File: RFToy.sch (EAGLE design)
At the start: 33 parts, among them IC1 ATMEGA328P, IC4 CH340G, J1 AYZ0202, X1 USBSMD, X2 12MHz

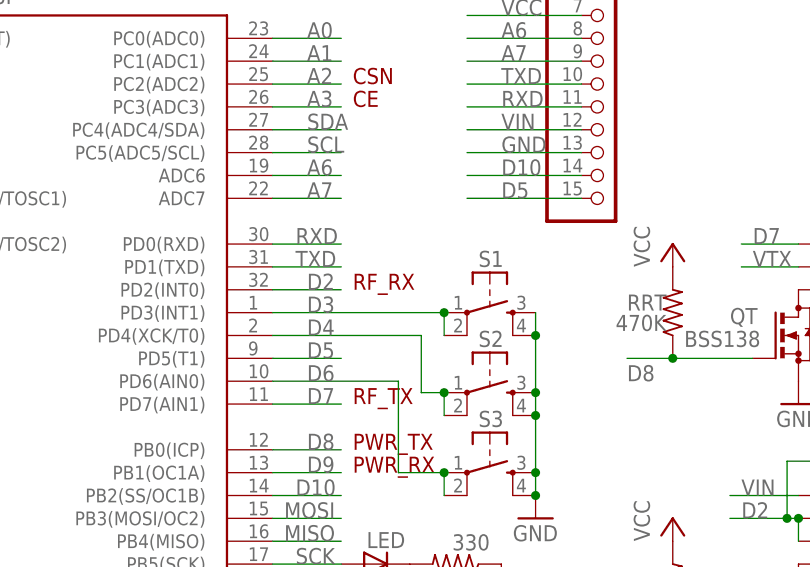
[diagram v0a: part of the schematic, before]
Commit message: correct pin assignments
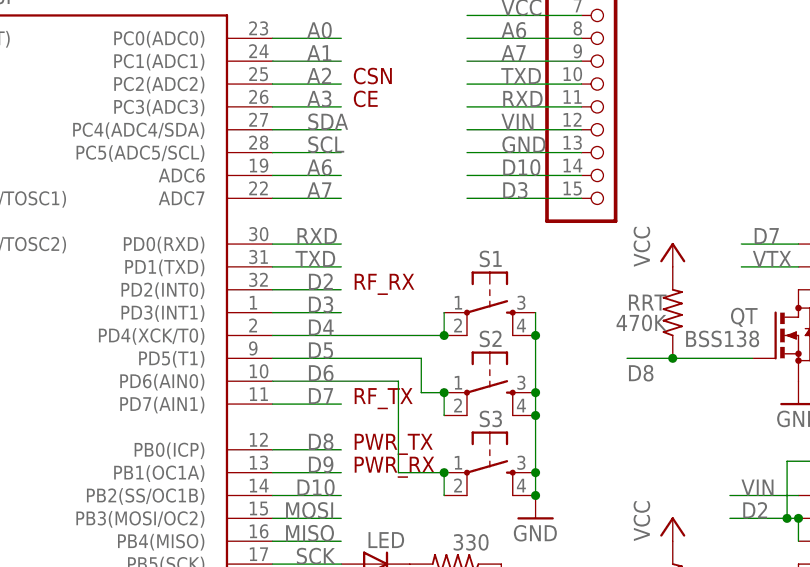
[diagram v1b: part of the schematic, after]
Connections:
- net D3: now also JP6.15; no longer S1.1, S1.2
- net D4: now also S1.1, S1.2; no longer S2.1, S2.2
- net D5: now also S2.1, S2.2; no longer JP6.15
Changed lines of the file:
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@@
 <setting verticaltext="up"/>
 </settings>
-<grid distance="0.05" unitdist="inch" unit="inch" style="lines" multiple="1" display="no" altdistance="0.01" altunitdist="inch" altunit="inch"/>
+<grid distance="0.1" unitdist="inch" unit="inch" style="lines" multiple="1" display="no" altdistance="0.01" altunitdist="inch" altunit="inch"/>
 <layers>
 <layer number="1" name="Top" color="4" fill="1" visible="no" active="no"/>
@@
 <pinref part="S3" gate="S" pin="4"/>
 <junction x="91.44" y="11.43"/>
-<wire x1="91.44" y1="31.75" x2="91.44" y2="29.21" width="0.1524" layer="91"/>
 <pinref part="S1" gate="S" pin="3"/>
 <pinref part="S1" gate="S" pin="4"/>
+<wire x1="91.44" y1="31.75" x2="91.44" y2="29.21" width="0.1524" layer="91"/>
 <wire x1="91.44" y1="29.21" x2="91.44" y2="22.86" width="0.1524" layer="91"/>
 <junction x="91.44" y="29.21"/>
@@
 </segment>
 </net>
-<net name="D4" class="0">
-<segment>
-<pinref part="IC1" gate="G$1" pin="PD4(XCK/T0)"/>
-<label x="66.04" y="29.21" size="1.778" layer="95"/>
-<wire x1="62.23" y1="29.21" x2="78.74" y2="29.21" width="0.1524" layer="91"/>
-<wire x1="78.74" y1="29.21" x2="78.74" y2="22.86" width="0.1524" layer="91"/>
-<wire x1="81.28" y1="22.86" x2="81.28" y2="20.32" width="0.1524" layer="91"/>
-<pinref part="S2" gate="S" pin="1"/>
-<pinref part="S2" gate="S" pin="2"/>
-<wire x1="78.74" y1="22.86" x2="81.28" y2="22.86" width="0.1524" layer="91"/>
-<junction x="81.28" y="22.86"/>
-</segment>
-</net>
 <net name="D8" class="0">
 <segment>
@@
 <junction x="106.68" y="26.67"/>
 <label x="101.6" y="24.13" size="1.778" layer="95"/>
-</segment>
-</net>
-<net name="D3" class="0">
-<segment>
-<pinref part="IC1" gate="G$1" pin="PD3(INT1)"/>
-<label x="66.04" y="31.75" size="1.778" layer="95"/>
-<pinref part="S1" gate="S" pin="1"/>
-<wire x1="81.28" y1="31.75" x2="81.28" y2="29.21" width="0.1524" layer="91"/>
-<pinref part="S1" gate="S" pin="2"/>
-<wire x1="62.23" y1="31.75" x2="81.28" y2="31.75" width="0.1524" layer="91"/>
-<junction x="81.28" y="31.75"/>
 </segment>
 </net>
@@
 <segment>
 <pinref part="IC1" gate="G$1" pin="PD5(T1)"/>
-<wire x1="62.23" y1="26.67" x2="69.85" y2="26.67" width="0.1524" layer="91"/>
 <label x="66.04" y="26.67" size="1.778" layer="95"/>
+<wire x1="81.28" y1="22.86" x2="81.28" y2="20.32" width="0.1524" layer="91"/>
+<pinref part="S2" gate="S" pin="1"/>
+<pinref part="S2" gate="S" pin="2"/>
+<wire x1="78.74" y1="22.86" x2="81.28" y2="22.86" width="0.1524" layer="91"/>
+<junction x="81.28" y="22.86"/>
+<wire x1="62.23" y1="26.67" x2="78.74" y2="26.67" width="0.1524" layer="91"/>
+<wire x1="78.74" y1="26.67" x2="78.74" y2="22.86" width="0.1524" layer="91"/>
+</segment>
+</net>
+<net name="IRQ" class="0">
+<segment>
+<pinref part="JP5" gate="A" pin="8"/>
+<wire x1="100.33" y1="115.57" x2="110.49" y2="115.57" width="0.1524" layer="91"/>
+<label x="105.41" y="115.57" size="1.778" layer="95"/>
+</segment>
+</net>
+<net name="D4" class="0">
+<segment>
+<pinref part="IC1" gate="G$1" pin="PD4(XCK/T0)"/>
+<label x="66.04" y="29.21" size="1.778" layer="95"/>
+<pinref part="S1" gate="S" pin="1"/>
+<pinref part="S1" gate="S" pin="2"/>
+<wire x1="81.28" y1="31.75" x2="81.28" y2="29.21" width="0.1524" layer="91"/>
+<wire x1="62.23" y1="29.21" x2="81.28" y2="29.21" width="0.1524" layer="91"/>
+<junction x="81.28" y="29.21"/>
+</segment>
+</net>
+<net name="D3" class="0">
+<segment>
+<pinref part="IC1" gate="G$1" pin="PD3(INT1)"/>
+<wire x1="62.23" y1="31.75" x2="69.85" y2="31.75" width="0.1524" layer="91"/>
+<label x="66.04" y="31.75" size="1.778" layer="95"/>
 </segment>
 <segment>
@@
 </segment>
 </net>
-<net name="IRQ" class="0">
-<segment>
-<pinref part="JP5" gate="A" pin="8"/>
-<wire x1="100.33" y1="115.57" x2="110.49" y2="115.57" width="0.1524" layer="91"/>
-<label x="105.41" y="115.57" size="1.778" layer="95"/>
-</segment>
-</net>
